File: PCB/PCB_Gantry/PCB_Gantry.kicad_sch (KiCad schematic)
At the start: 14 parts

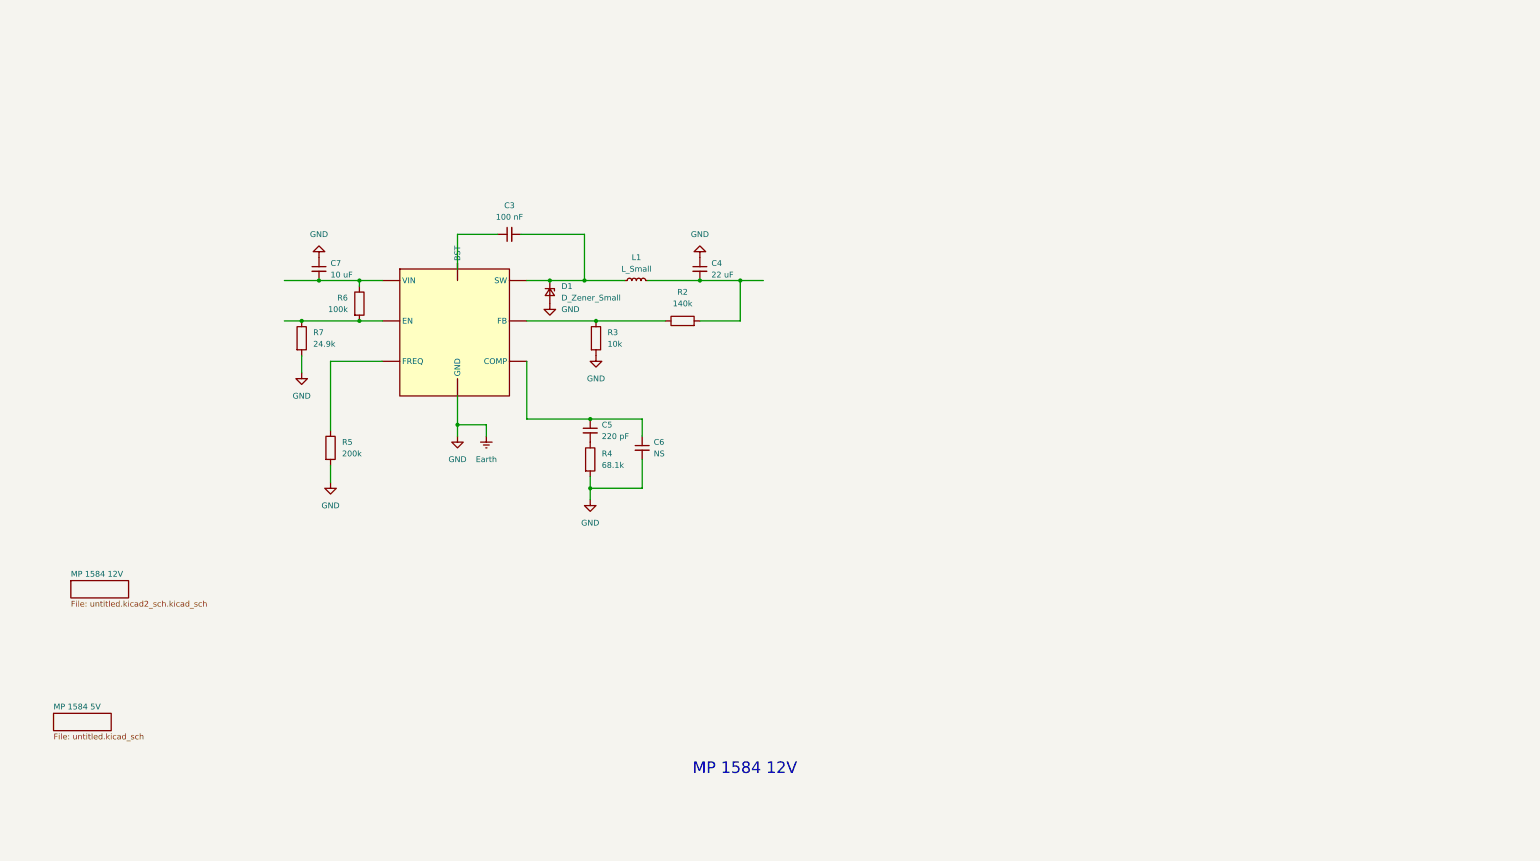
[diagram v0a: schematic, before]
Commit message: Added Schematic
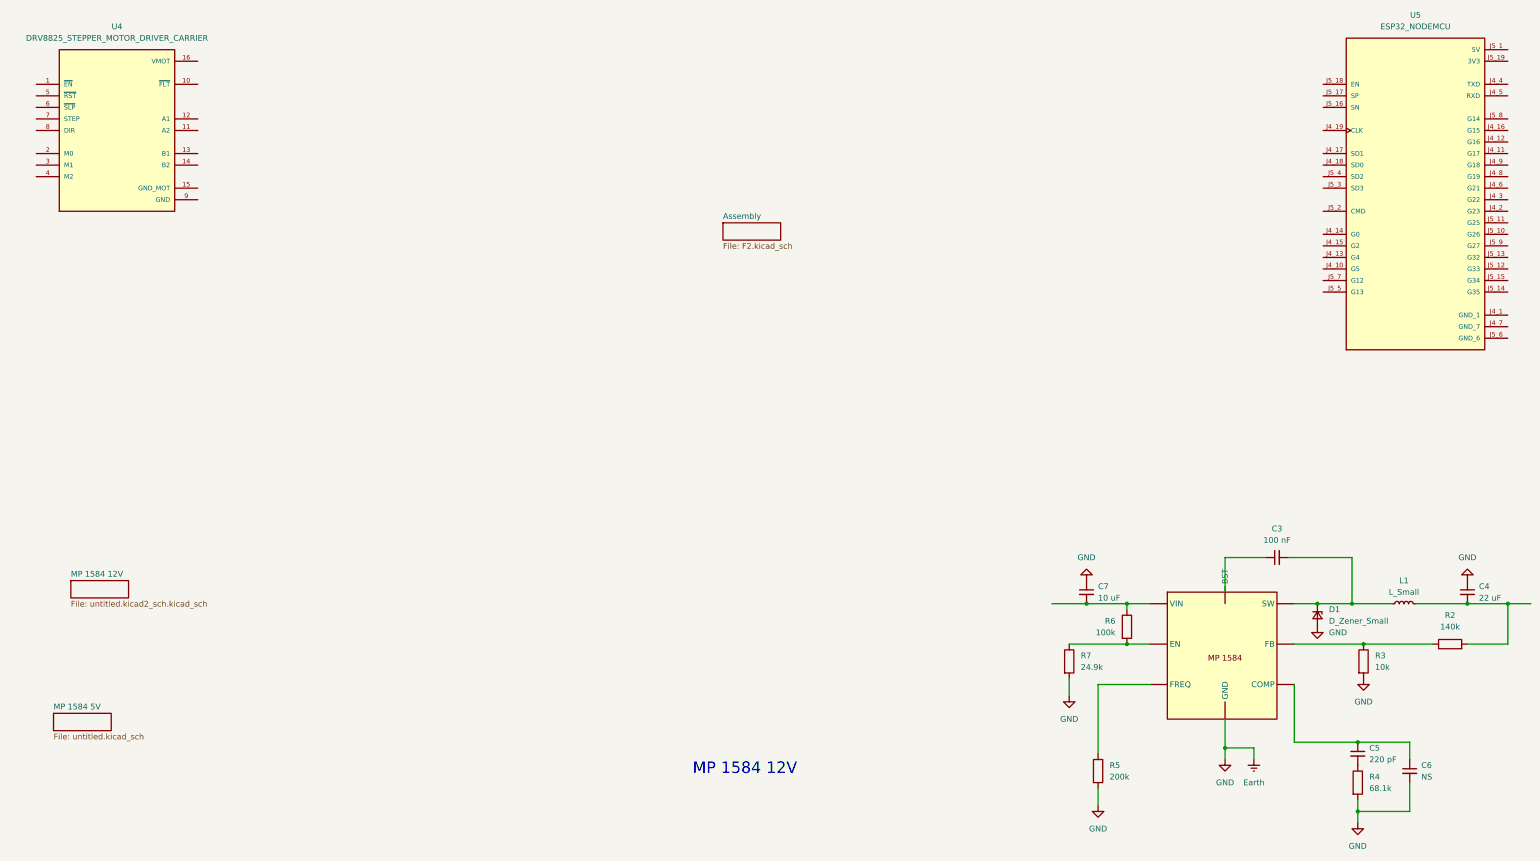
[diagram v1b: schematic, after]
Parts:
- added U4: DRV8825_STEPPER_MOTOR_DRIVER_CARRIER, DRV8825_STEPPER_MOTOR_DRIVER_CARRIER:IC_DRV8825_STEPPER_MOTOR_DRIVER_CARRIER, symbol DRV8825_STEPPER_MOTOR_DRIVER_CARRIER:DRV8825_STEPPER_MOTOR_DRIVER_CARRIER
- added U5: ESP32_NODEMCU, ESP32_NODEMCU:MODULE_ESP32_NODEMCU, symbol ESP32_NODEMCU:ESP32_NODEMCU
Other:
- added sheet Assembly (F2.kicad_sch)
- moved on the sheet: C3, C4, C5, C6, C7, D1, L1, R2, R3, R4, R5, R6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
